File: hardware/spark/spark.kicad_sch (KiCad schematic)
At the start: 17 parts, among them Q1 PNP, Q2 NPN

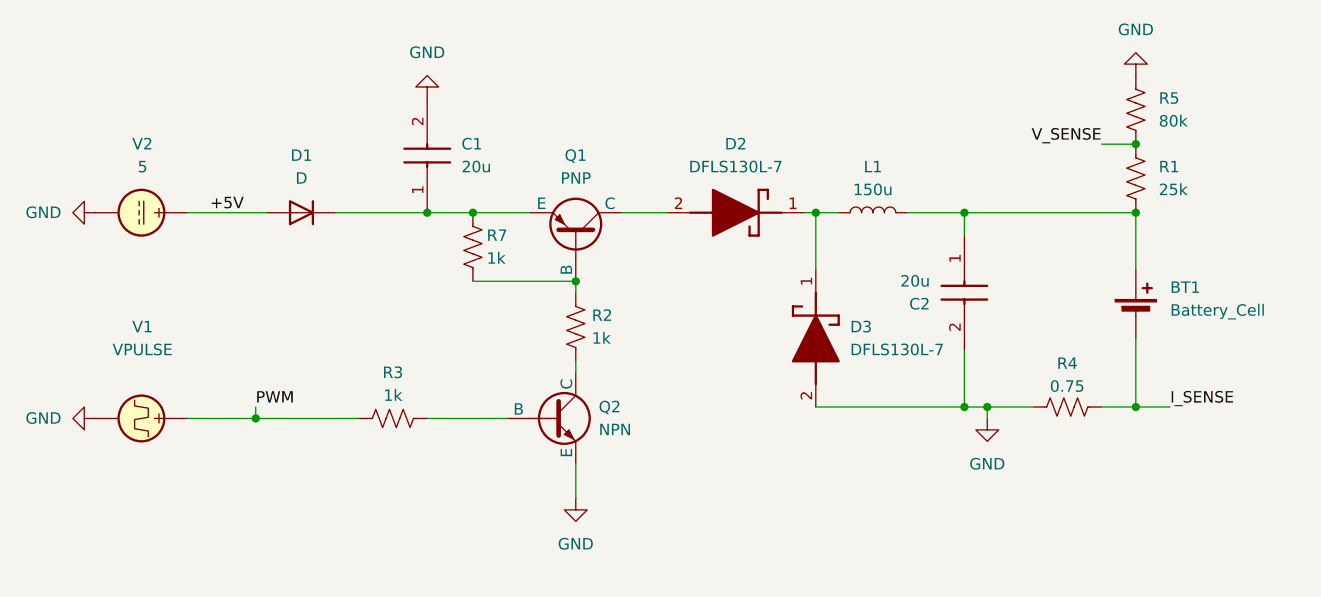
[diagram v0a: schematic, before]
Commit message: Add library components and layout basics
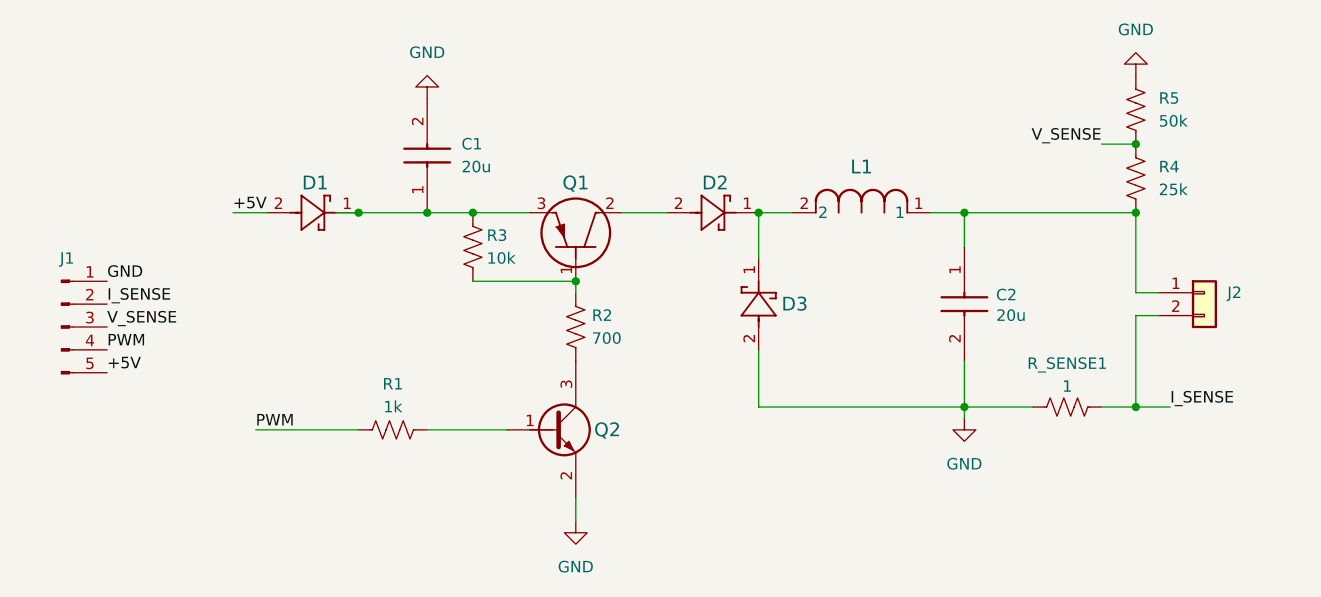
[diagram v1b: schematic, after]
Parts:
- removed BT1: Battery_Cell, symbol Device:Battery_Cell
- removed D1: D, symbol Device:D
- removed D2, D3: DFLS130L-7, DFLS130L7, symbol DFLS130L-7:DFLS130L-7
- removed L1: 150u, symbol Device:L
- removed Q1: PNP, symbol Simulation_SPICE:PNP
- removed Q2: NPN, symbol Simulation_SPICE:NPN
- removed V1: VPULSE, symbol Simulation_SPICE:VPULSE
- removed V2: 5, symbol Simulation_SPICE:VDC
- added D1, D2, D3: MBR120VLSFT1G, SDO_SOD-123FL_ONS, symbol MBR120VLSFT1G:MBR120VLSFT1G
- added J1: Conn_01x05_Pin, Connector_PinHeader_2.54mm:PinHeader_1x05_P2.54mm_Vertical, symbol Connector:Conn_01x05_Pin
- added J2: Conn_01x02, Connector_PinHeader_2.54mm:PinHeader_1x02_P2.54mm_Vertical, symbol Connector_Generic:Conn_01x02
- added L1: SRR1260-151K, IND_BOURNS_SRR1260, symbol SRR1260-151:SRR1260-151K
- added Q1: STD2805T4, DPAKTO-252_TYPEA_STM, symbol STD28054:STD2805T4
- added Q2: PMBT2369, SOT23_NXP, symbol PMBT2369:PMBT2369
- C1, C2: footprint GRMJN7 -> GRMJN7:DIOM7959X262N
- R1: renamed from R3; footprint (none) -> Resistor_SMD:R_0402_1005Metric
- R2: value 1k -> 700; footprint (none) -> Resistor_SMD:R_0402_1005Metric
- R3: renamed from R7; value 1k -> 10k; footprint (none) -> Resistor_SMD:R_0402_1005Metric
- R4: renamed from R1; footprint (none) -> Resistor_SMD:R_0402_1005Metric
- R5: value 80k -> 50k; footprint (none) -> Resistor_SMD:R_0402_1005Metric
- R_SENSE1: renamed from R4; value 0.75 -> 1; footprint (none) -> Resistor_SMD:R_0402_1005Metric
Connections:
- net +5V: now also D1.2, J1.5 (Pin_5)
- net GND: now also D3.2, J1.1 (Pin_1), Q2.2
- net I_SENSE: now also J1.2 (Pin_2), J2.2 (Pin_2)
- net PWM: now also J1.4 (Pin_4)
- net V_SENSE: now also J1.3 (Pin_3)
- net at C1.1, R3.1: now also D1.1, Q1.3
- net at R2.2: now also Q2.3
- net at R1.2: now also Q2.1
- net at R2.1, R3.2: now also Q1.1
- net at C2.1, R4.2: now also J2.1 (Pin_1), L1.1
- new net: D2.1, D3.1, L1.2
- new net: D2.2, Q1.2
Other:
- moved on the sheet: C2, R1
